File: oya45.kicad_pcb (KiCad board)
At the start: 2 copper layers, 94 parts, among them U1 ProMicro

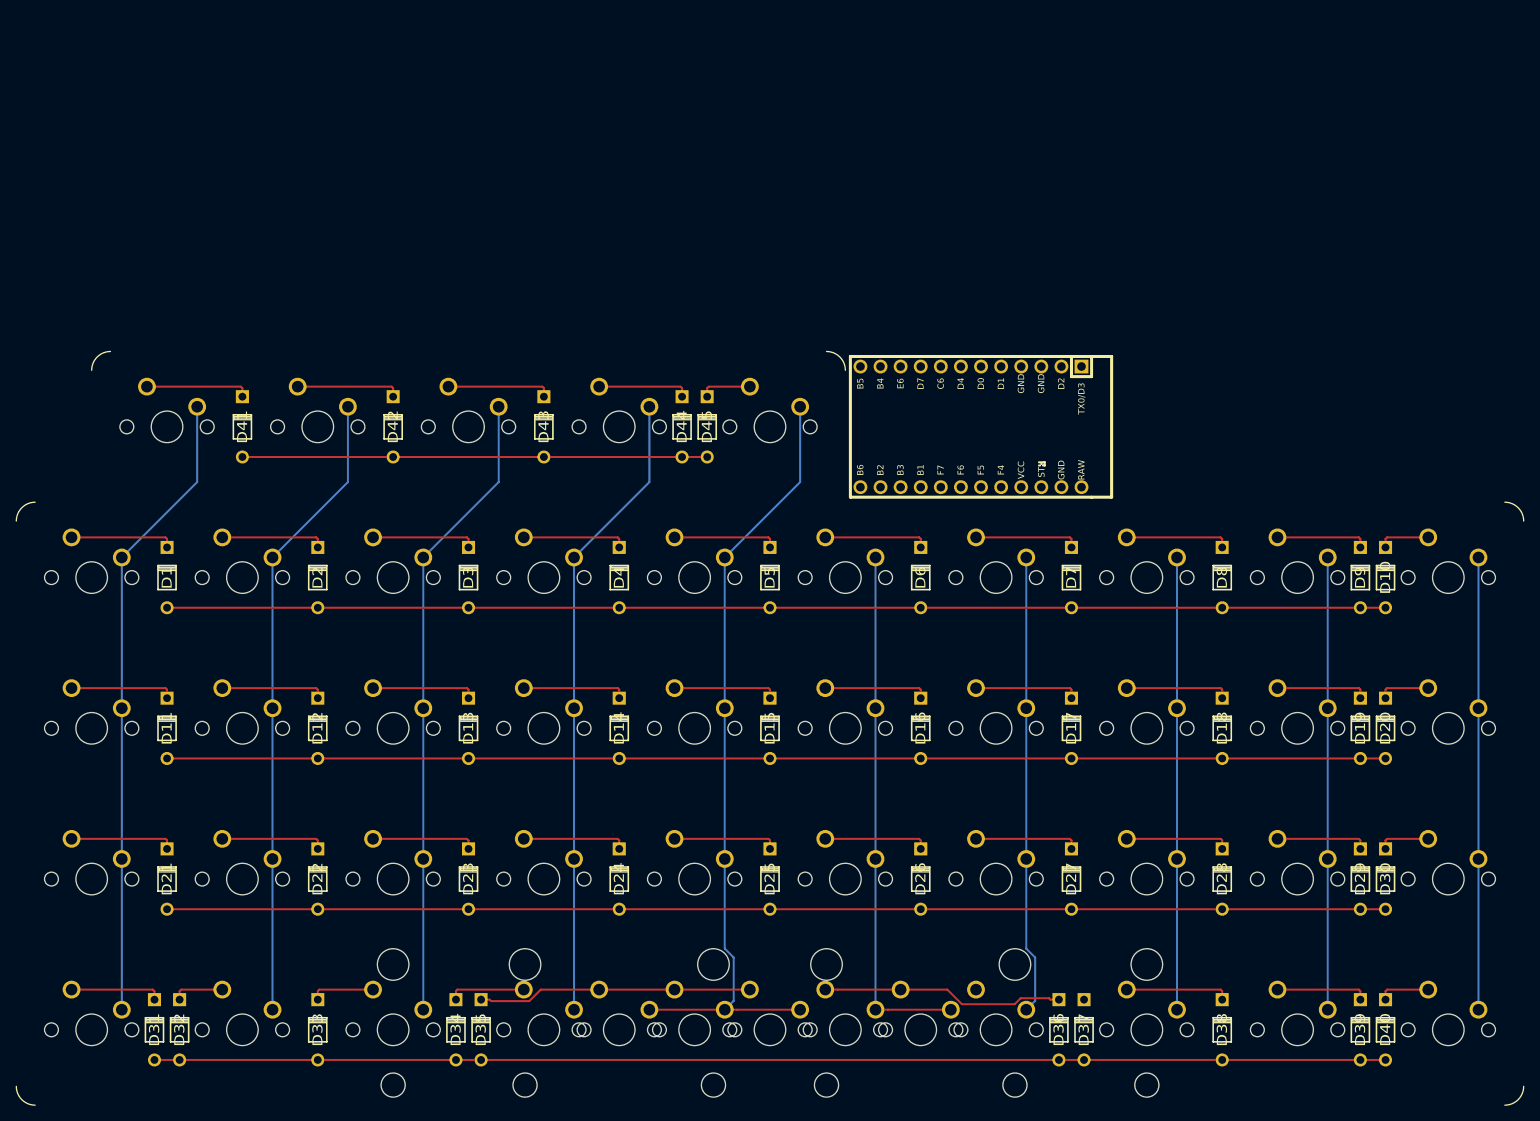
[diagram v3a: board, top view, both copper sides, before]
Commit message: route final fixed; first route
first route, could route cleaner
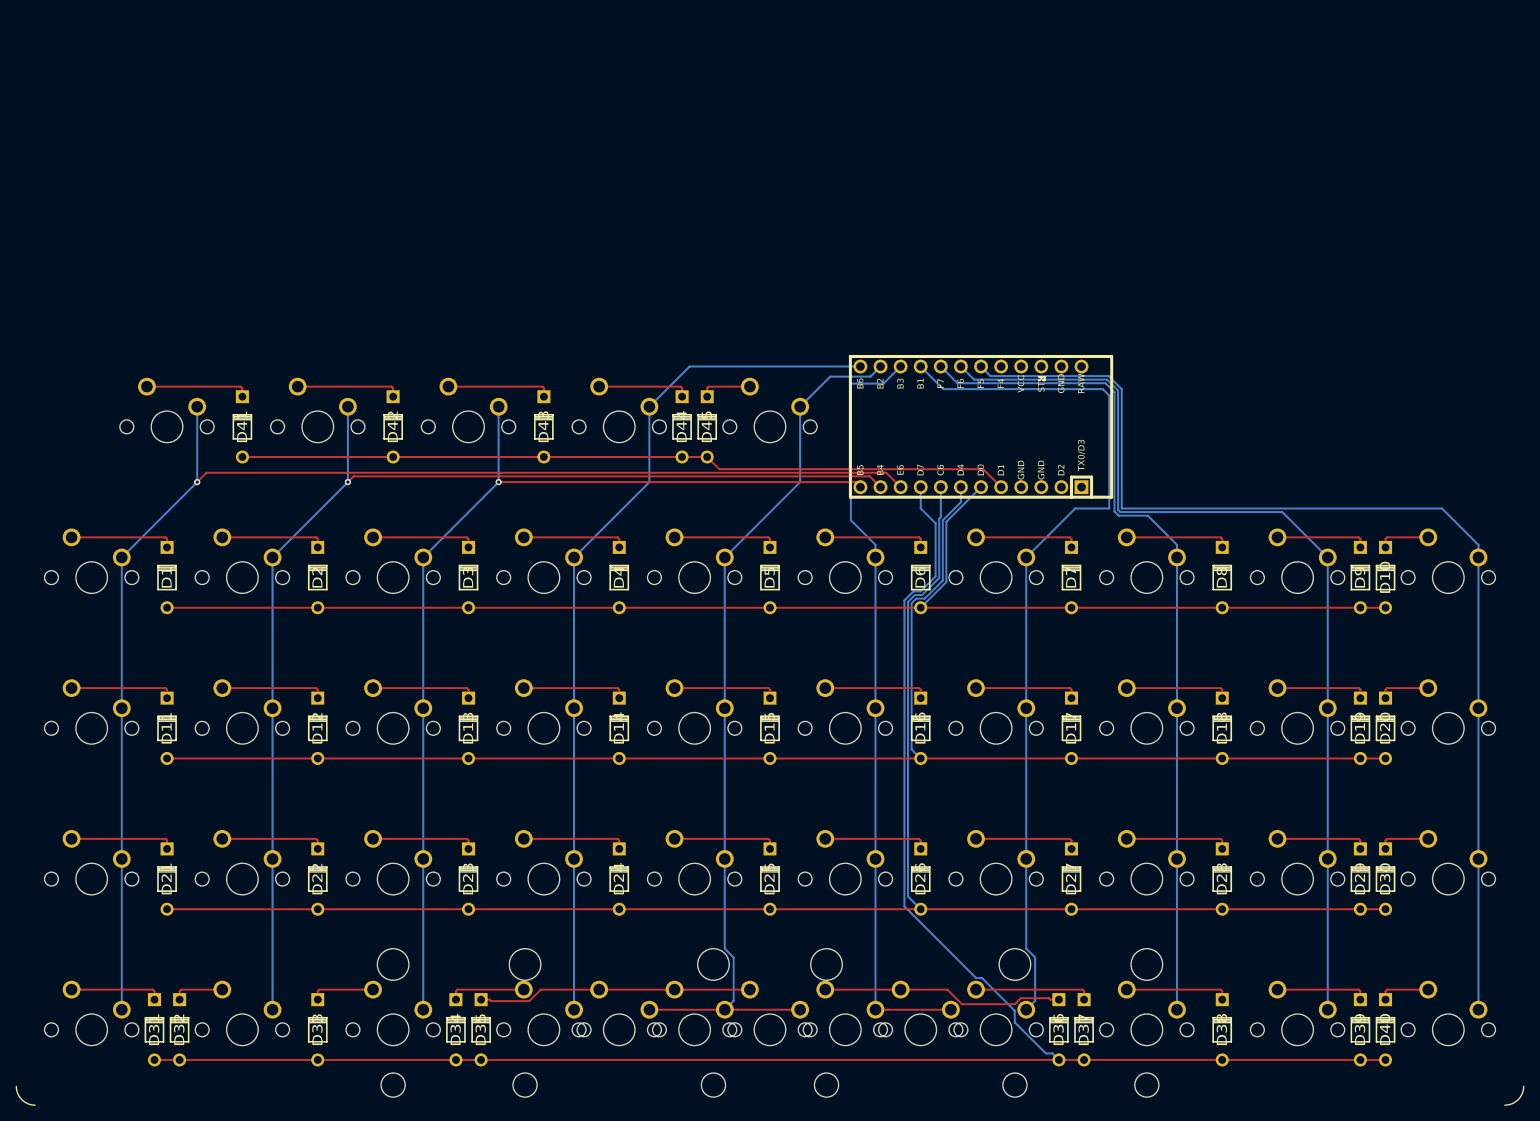
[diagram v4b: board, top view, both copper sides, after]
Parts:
- U1: moved to B.Cu
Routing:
- net col0: track 80.1 -> 170.3 mm, vias 0 -> 1
- net row4: track 155.6 -> 239.9 mm
- net col9: track 57.2 -> 139.8 mm
- net col1: track 80.1 -> 148.3 mm, vias 0 -> 1
- net col8: track 57.2 -> 122.3 mm
- net row3: track 154.0 -> 210.2 mm
- net col6: track 58.1 -> 110.7 mm
- net col7: track 57.2 -> 106.8 mm
- net col2: track 80.1 -> 126.1 mm, vias 0 -> 1
- net row0: track 58.7 -> 97.5 mm
- net row2: track 154.0 -> 192.0 mm
- net col5: track 66.7 -> 97.1 mm
- net col3: track 80.1 -> 108.9 mm
- net row1: track 154.0 -> 172.4 mm
- net Net-(D37-Pad2): track 0.00 -> 14.8 mm
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
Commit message: pro micro first clean routing
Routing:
- net col0: track 170.3 -> 83.1 mm
- net col9: track 139.8 -> 65.2 mm
- net col8: track 122.3 -> 65.3 mm
- net col6: track 110.7 -> 58.1 mm
- net col7: track 106.8 -> 58.7 mm
- net row0: track 97.5 -> 60.9 mm
- net row1: track 172.4 -> 158.6 mm
- net row2: track 192.0 -> 179.2 mm
- net row4: track 239.9 -> 227.9 mm
- net row3: track 210.2 -> 198.7 mm
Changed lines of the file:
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@@
     (thickness 1.6)
     (drawings 8)
-    (tracks 271)
+    (tracks 231)
     (zones 0)
     (modules 94)
@@
   (segment (start 162.750499 60.134501) (end 161.925 60.96) (width 0.254) (layer B.Cu) (net 1))
   (segment (start 165.167999 57.717001) (end 162.750499 60.134501) (width 0.254) (layer B.Cu) (net 1))
-  (segment (start 165.167999 50.097001) (end 165.167999 57.717001) (width 0.254) (layer B.Cu) (net 1))
-  (segment (start 169.545 45.72) (end 165.167999 50.097001) (width 0.254) (layer B.Cu) (net 1))
   (segment (start 66.675 52.2605) (end 66.675 53.34) (width 0.254) (layer F.Cu) (net 2))
   (segment (start 66.4845 52.07) (end 66.675 52.2605) (width 0.254) (layer F.Cu) (net 2))
@@
   (segment (start 160.772499 60.406799) (end 160.772499 78.857499) (width 0.254) (layer B.Cu) (net 12))
   (segment (start 161.099501 79.184501) (end 161.925 80.01) (width 0.254) (layer B.Cu) (net 12))
-  (segment (start 167.005 45.72) (end 167.005 47.617934) (width 0.254) (layer B.Cu) (net 12))
-  (segment (start 167.005 47.617934) (end 164.713989 49.908945) (width 0.254) (layer B.Cu) (net 12))
-  (segment (start 164.713989 49.908945) (end 164.713989 57.528945) (width 0.254) (layer B.Cu) (net 12))
   (segment (start 164.713989 57.528945) (end 162.435435 59.807499) (width 0.254) (layer B.Cu) (net 12))
   (segment (start 162.435435 59.807499) (end 161.371799 59.807499) (width 0.254) (layer B.Cu) (net 12))
@@
   (segment (start 160.318489 97.453489) (end 161.925 99.06) (width 0.254) (layer B.Cu) (net 23))
   (segment (start 160.318489 60.218742) (end 160.318489 97.453489) (width 0.254) (layer B.Cu) (net 23))
-  (segment (start 164.465 49.515867) (end 164.259979 49.720888) (width 0.254) (layer B.Cu) (net 23))
-  (segment (start 164.465 45.72) (end 164.465 49.515867) (width 0.254) (layer B.Cu) (net 23))
-  (segment (start 164.259979 49.720888) (end 164.259979 57.196271) (width 0.254) (layer B.Cu) (net 23))
   (segment (start 164.259979 57.196271) (end 162.102761 59.353489) (width 0.254) (layer B.Cu) (net 23))
   (segment (start 162.102761 59.353489) (end 161.183742 59.353489) (width 0.254) (layer B.Cu) (net 23))
@@
   (segment (start 168.927297 107.767999) (end 169.680499 107.767999) (width 0.254) (layer B.Cu) (net 34))
   (segment (start 159.864479 98.705181) (end 168.927297 107.767999) (width 0.254) (layer B.Cu) (net 34))
-  (segment (start 163.805969 50.299719) (end 163.805969 57.008215) (width 0.254) (layer B.Cu) (net 34))
   (segment (start 169.680499 107.767999) (end 173.807999 111.895499) (width 0.254) (layer B.Cu) (net 34))
   (segment (start 161.914705 58.899479) (end 160.995685 58.899479) (width 0.254) (layer B.Cu) (net 34))
-  (segment (start 161.925 48.41875) (end 163.805969 50.299719) (width 0.254) (layer B.Cu) (net 34))
   (segment (start 177.735539 117.284501) (end 178.562001 117.284501) (width 0.254) (layer B.Cu) (net 34))
-  (segment (start 161.925 45.72) (end 161.925 48.41875) (width 0.254) (layer B.Cu) (net 34))
   (segment (start 65.0875 109.4105) (end 65.0875 110.49) (width 0.254) (layer F.Cu) (net 35))
   (segment (start 64.897 109.22) (end 65.0875 109.4105) (width 0.254) (layer F.Cu) (net 35))
@@
   (segment (start 226.06 109.22) (end 220.853 109.22) (width 0.254) (layer F.Cu) (net 44))
   (segment (start 76.2 41.91) (end 134.9375 41.91) (width 0.254) (layer F.Cu) (net 45))
-  (segment (start 169.81498 43.44998) (end 172.085 45.72) (width 0.254) (layer F.Cu) (net 45))
   (segment (start 134.9375 41.91) (end 136.47748 43.44998) (width 0.254) (layer F.Cu) (net 45))
-  (segment (start 136.47748 43.44998) (end 169.81498 43.44998) (width 0.254) (layer F.Cu) (net 45))
   (segment (start 76.2 33.2105) (end 76.2 34.29) (width 0.254) (layer F.Cu) (net 46))
   (segment (start 76.0095 33.02) (end 76.2 33.2105) (width 0.254) (layer F.Cu) (net 46))
@@
   (via (at 70.485 45.085) (size 0.8) (drill 0.4) (layers F.Cu B.Cu) (net 51))
   (segment (start 158.508701 44.843701) (end 159.385 45.72) (width 0.254) (layer F.Cu) (net 51))
-  (segment (start 157.56899 43.90399) (end 158.508701 44.843701) (width 0.254) (layer F.Cu) (net 51))
-  (segment (start 71.66601 43.90399) (end 157.56899 43.90399) (width 0.254) (layer F.Cu) (net 51))
   (segment (start 70.485 45.085) (end 71.66601 43.90399) (width 0.254) (layer F.Cu) (net 51))
   (segment (start 89.535 45.085) (end 80.01 54.61) (width 0.254) (layer B.Cu) (net 52))
@@
   (segment (start 175.26 104.038816) (end 176.384999 105.163815) (width 0.254) (layer B.Cu) (net 57))
   (segment (start 175.26 54.61) (end 175.26 104.038816) (width 0.254) (layer B.Cu) (net 57))
-  (segment (start 161.925 30.48) (end 164.7825 33.3375) (width 0.254) (layer B.Cu) (net 57))
-  (segment (start 164.7825 33.3375) (end 184.94375 33.3375) (width 0.254) (layer B.Cu) (net 57))
-  (segment (start 184.94375 33.3375) (end 185.7375 34.13125) (width 0.254) (layer B.Cu) (net 57))
-  (segment (start 185.7375 34.13125) (end 185.7375 48.41875) (width 0.254) (layer B.Cu) (net 57))
-  (segment (start 181.45125 48.41875) (end 175.26 54.61) (width 0.254) (layer B.Cu) (net 57))
-  (segment (start 185.7375 48.41875) (end 181.45125 48.41875) (width 0.254) (layer B.Cu) (net 57))
   (segment (start 194.31 54.61) (end 194.31 111.76) (width 0.254) (layer B.Cu) (net 58))
-  (segment (start 186.948886 49.32677) (end 186.41698 48.794864) (width 0.254) (layer B.Cu) (net 58))
-  (segment (start 190.61776 49.32677) (end 186.948886 49.32677) (width 0.254) (layer B.Cu) (net 58))
   (segment (start 194.31 54.61) (end 194.31 53.01901) (width 0.254) (layer B.Cu) (net 58))
-  (segment (start 194.31 53.01901) (end 190.61776 49.32677) (width 0.254) (layer B.Cu) (net 58))
-  (segment (start 186.41698 48.794864) (end 186.41698 33.713612) (width 0.254) (layer B.Cu) (net 58))
-  (segment (start 186.41698 33.713612) (end 185.294689 32.591321) (width 0.254) (layer B.Cu) (net 58))
-  (segment (start 166.576321 32.591321) (end 164.465 30.48) (width 0.254) (layer B.Cu) (net 58))
-  (segment (start 185.294689 32.591321) (end 166.576321 32.591321) (width 0.254) (layer B.Cu) (net 58))
   (segment (start 213.36 54.61) (end 213.36 111.76) (width 0.254) (layer B.Cu) (net 59))
-  (segment (start 168.662311 32.137311) (end 185.482745 32.137311) (width 0.254) (layer B.Cu) (net 59))
-  (segment (start 167.005 30.48) (end 168.662311 32.137311) (width 0.254) (layer B.Cu) (net 59))
-  (segment (start 185.482745 32.137311) (end 186.87099 33.525556) (width 0.254) (layer B.Cu) (net 59))
   (segment (start 207.62276 48.87276) (end 213.36 54.61) (width 0.254) (layer B.Cu) (net 59))
-  (segment (start 186.87099 33.525556) (end 186.87099 48.606807) (width 0.254) (layer B.Cu) (net 59))
-  (segment (start 186.87099 48.606807) (end 187.136943 48.87276) (width 0.254) (layer B.Cu) (net 59))
-  (segment (start 187.136943 48.87276) (end 207.62276 48.87276) (width 0.254) (layer B.Cu) (net 59))
   (segment (start 232.41 54.61) (end 232.41 111.76) (width 0.254) (layer B.Cu) (net 60))
   (segment (start 232.41 53.01901) (end 227.80974 48.41875) (width 0.254) (layer B.Cu) (net 60))
   (segment (start 232.41 54.61) (end 232.41 53.01901) (width 0.254) (layer B.Cu) (net 60))
-  (segment (start 227.80974 48.41875) (end 187.325 48.41875) (width 0.254) (layer B.Cu) (net 60))
-  (segment (start 187.325 48.41875) (end 187.325 33.3375) (width 0.254) (layer B.Cu) (net 60))
-  (segment (start 170.421299 31.356299) (end 169.545 30.48) (width 0.254) (layer B.Cu) (net 60))
-  (segment (start 170.748301 31.683301) (end 170.421299 31.356299) (width 0.254) (layer B.Cu) (net 60))
-  (segment (start 185.670801 31.683301) (end 170.748301 31.683301) (width 0.254) (layer B.Cu) (net 60))
-  (segment (start 187.325 33.3375) (end 185.670801 31.683301) (width 0.254) (layer B.Cu) (net 60))
 )
